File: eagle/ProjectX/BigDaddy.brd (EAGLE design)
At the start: 100 x 100 mm, 180 parts, among them U10 TC4427AEOA, U11 TC4427AEOA, U12 TC4427AEOA, U13 TC4427AEOA, U19 TC4427AEOA, U20 TC4427AEOA, U21 TC4427AEOA, U22 TC4427AEOA, U23 TC4427AEOA, U24 TC4427AEOA, U25 TC4427AEOA, U26 TC4427AEOA, U27 TC4427AEOA, U28 TC4427AEOA, U29 TC4427AEOA, U3 TC4427AEOA, U30 TC4427AEOA, U31 TC4427AEOA, U32 TC4427AEOA, U34 TC4427AEOA, U35 TC4427AEOA, U36 TC4427AEOA, U37 TC4427AEOA, U38 TC4427AEOA, U39 TC4427AEOA, U4 TC4427AEOA, U40 TC4427AEOA, U41 TC4427AEOA, U42 TC4427AEOA, U43 TC4427AEOA, U44 TC4427AEOA, U45 TC4427AEOA, U5 TC4427AEOA, U55 TC4427AEOA, U56 TC4427AEOA, U57 TC4427AEOA, U58 TC4427AEOA, U59 TC4427AEOA, U60 TC4427AEOA, U61 TC4427AEOA, U62 TC4427AEOA, U63 TC4427AEOA, U7 TC4427AEOA, U9 TC4427AEOA

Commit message: More work on the board
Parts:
- moved J2 23.0 mm to (24.0, 98.5), turned to 0 degrees
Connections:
- new net 1: DIP1.2, U28.4
- new net 2: DIP1.4, U28.2
- new net 3: DIP1.3, U29.4
- new net 4: DIP1.5, U29.2
- new net N$1: DIP1.203, J2.1
- new net N$13: DIP1.190, J2.5
- new net N$14: DIP1.187, J2.6
- new net N$17: DIP1.185, J2.7
- new net N$18: DIP1.180, J2.8
- new net N$2: DIP1.200, J2.2
- new net N$29: DIP1.178, J2.9
- new net N$3: DIP1.197, J2.3
- new net N$30: DIP1.172, J2.10
- new net N$4: DIP1.193, J2.4
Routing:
- net 3: track 0.00 -> 16.4 mm
- net 1: track 0.00 -> 16.1 mm
- net 2: track 0.00 -> 10.3 mm
- net 4: track 0.00 -> 9.98 mm
- net N$30: track 0.00 -> 6.66 mm
- net N$29: track 0.00 -> 6.43 mm
- net N$18: track 0.00 -> 5.87 mm
- net N$17: track 0.00 -> 4.88 mm
- net N$14: track 0.00 -> 4.22 mm
- net N$3: track 0.00 -> 4.18 mm
- net N$13: track 0.00 -> 3.99 mm
- net N$4: track 0.00 -> 3.77 mm
- net N$2: track 0.00 -> 3.64 mm
- net N$1: track 0.00 -> 3.10 mm
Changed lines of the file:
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@@
 <element name="J1" library="SparkFun-Connectors" library_urn="urn:adsk.eagle:library:513" package="1X02_LOCK_LONGPADS" package3d_urn="urn:adsk.eagle:package:38047/1" value="" x="68.75" y="10" rot="R180"/>
 <element name="U$1" library="Parts" package="OKI-78SR-HORIZ" value="OKI-78SR" x="67.5" y="30" rot="R180"/>
-<element name="J2" library="SparkFun-Connectors" library_urn="urn:adsk.eagle:library:513" package="1X10" package3d_urn="urn:adsk.eagle:package:38157/1" value="" x="47" y="98.5" rot="R180">
-<attribute name="PROD_ID" value="CONN-11563" x="47" y="98.5" size="1.778" layer="27" rot="R180" display="off"/>
+<element name="J2" library="SparkFun-Connectors" library_urn="urn:adsk.eagle:library:513" package="1X10" package3d_urn="urn:adsk.eagle:package:38157/1" value="" x="24" y="98.5">
+<attribute name="PROD_ID" value="CONN-11563" x="24" y="98.5" size="1.778" layer="27" display="off"/>
 </element>
 </elements>
@@
 <wire x1="50" y1="82.6378" x2="50" y2="82.5" width="0.508" layer="1"/>
 </signal>
+<signal name="N$1">
+<contactref element="J2" pad="1"/>
+<contactref element="DIP1" pad="203"/>
+<wire x1="24" y1="98.5" x2="24" y2="95.4" width="0.254" layer="1"/>
+</signal>
+<signal name="N$2">
+<contactref element="J2" pad="2"/>
+<contactref element="DIP1" pad="200"/>
+<wire x1="26.54" y1="98.5" x2="26" y2="98.5" width="0.254" layer="1"/>
+<wire x1="26" y1="98.5" x2="26" y2="95.4" width="0.254" layer="1"/>
+</signal>
+<signal name="N$3">
+<contactref element="J2" pad="3"/>
+<contactref element="DIP1" pad="197"/>
+<wire x1="29.08" y1="98.5" x2="28" y2="98.5" width="0.254" layer="1"/>
+<wire x1="28" y1="98.5" x2="28" y2="95.4" width="0.254" layer="1"/>
+</signal>
+<signal name="N$4">
+<contactref element="J2" pad="4"/>
+<contactref element="DIP1" pad="193"/>
+<wire x1="31.62" y1="98.5" x2="30" y2="96.88" width="0.254" layer="1"/>
+<wire x1="30" y1="96.88" x2="30" y2="95.4" width="0.254" layer="1"/>
+</signal>
+<signal name="N$13">
+<contactref element="J2" pad="5"/>
+<contactref element="DIP1" pad="190"/>
+<wire x1="34.16" y1="98.5" x2="32" y2="96.34" width="0.254" layer="1"/>
+<wire x1="32" y1="96.34" x2="32" y2="95.4" width="0.254" layer="1"/>
+</signal>
+<signal name="N$14">
+<contactref element="J2" pad="6"/>
+<contactref element="DIP1" pad="187"/>
+<wire x1="36.7" y1="98.5" x2="34" y2="95.8" width="0.254" layer="1"/>
+<wire x1="34" y1="95.8" x2="34" y2="95.4" width="0.254" layer="1"/>
+</signal>
+<signal name="N$17">
+<contactref element="J2" pad="7"/>
+<contactref element="DIP1" pad="185"/>
+<wire x1="39.24" y1="98.5" x2="38.49605625" y2="98.5" width="0.254" layer="1"/>
+<wire x1="36" y1="96.00394375" x2="36" y2="95.4" width="0.254" layer="1"/>
+<wire x1="38.49605625" y1="98.5" x2="36" y2="96.00394375" width="0.254" layer="1"/>
+</signal>
+<signal name="N$18">
+<contactref element="J2" pad="8"/>
+<contactref element="DIP1" pad="180"/>
+<wire x1="41.78" y1="98.5" x2="41.03605625" y2="98.5" width="0.254" layer="1"/>
+<wire x1="38" y1="96.77078125" x2="38" y2="95.4" width="0.254" layer="1"/>
+<wire x1="38.45921875" y1="97.23" x2="38" y2="96.77078125" width="0.254" layer="1"/>
+<wire x1="41.03605625" y1="98.5" x2="39.76605625" y2="97.23" width="0.254" layer="1"/>
+<wire x1="39.76605625" y1="97.23" x2="38.45921875" y2="97.23" width="0.254" layer="1"/>
+</signal>
+<signal name="N$29">
+<contactref element="J2" pad="9"/>
+<contactref element="DIP1" pad="178"/>
+<wire x1="40" y1="96.8173625" x2="40" y2="95.4" width="0.254" layer="1"/>
+<wire x1="44.32" y1="98.5" x2="43.57605625" y2="98.5" width="0.254" layer="1"/>
+<wire x1="40.4126375" y1="97.23" x2="40" y2="96.8173625" width="0.254" layer="1"/>
+<wire x1="43.57605625" y1="98.5" x2="42.30605625" y2="97.23" width="0.254" layer="1"/>
+<wire x1="42.30605625" y1="97.23" x2="40.4126375" y2="97.23" width="0.254" layer="1"/>
+</signal>
+<signal name="N$30">
+<contactref element="J2" pad="10"/>
+<contactref element="DIP1" pad="172"/>
+<wire x1="46.86" y1="98.5" x2="46.11605625" y2="98.5" width="0.254" layer="1"/>
+<wire x1="42" y1="96.2773625" x2="42" y2="95.4" width="0.254" layer="1"/>
+<wire x1="46.11605625" y1="98.5" x2="44.84605625" y2="97.23" width="0.254" layer="1"/>
+<wire x1="44.84605625" y1="97.23" x2="42.9526375" y2="97.23" width="0.254" layer="1"/>
+<wire x1="42.9526375" y1="97.23" x2="42" y2="96.2773625" width="0.254" layer="1"/>
+</signal>
+<signal name="1">
+<contactref element="U28" pad="4"/>
+<contactref element="DIP1" pad="2"/>
+<wire x1="20.8302" y1="94.163225" x2="20.636775" y2="93.9698" width="0.254" layer="1"/>
+<wire x1="20.636775" y1="93.9698" x2="19.363225" y2="93.9698" width="0.254" layer="1"/>
+<wire x1="9.095" y1="95.4" x2="9.095" y2="97.3622" width="0.254" layer="1"/>
+<wire x1="22" y1="95.4" x2="20.8302" y2="94.2302" width="0.254" layer="1"/>
+<wire x1="20.8302" y1="94.2302" x2="20.8302" y2="94.163225" width="0.254" layer="1"/>
+<wire x1="19.363225" y1="93.9698" x2="18.390225" y2="94.9428" width="0.254" layer="1"/>
+<wire x1="9.5522" y1="94.9428" x2="9.095" y2="95.4" width="0.254" layer="1"/>
+<wire x1="18.390225" y1="94.9428" x2="9.5522" y2="94.9428" width="0.254" layer="1"/>
+</signal>
+<signal name="2">
+<contactref element="U28" pad="2"/>
+<contactref element="DIP1" pad="4"/>
+<wire x1="20" y1="95.4" x2="11.635" y2="95.4" width="0.254" layer="1"/>
+<wire x1="11.635" y1="95.4" x2="11.635" y2="97.3622" width="0.254" layer="1"/>
+</signal>
+<signal name="3">
+<contactref element="U29" pad="4"/>
+<contactref element="DIP1" pad="3"/>
+<wire x1="20.8302" y1="91.836775" x2="20.636775" y2="92.0302" width="0.254" layer="1"/>
+<wire x1="20" y1="92.0302" x2="19.363225" y2="92.0302" width="0.254" layer="1"/>
+<wire x1="20" y1="92.0302" x2="20.636775" y2="92.0302" width="0.254" layer="1"/>
+<wire x1="22" y1="90.6" x2="20.8302" y2="91.7698" width="0.254" layer="1"/>
+<wire x1="20.8302" y1="91.7698" x2="20.8302" y2="91.836775" width="0.254" layer="1"/>
+<wire x1="9.095" y1="87.3622" x2="9.7554" y2="88.0226" width="0.254" layer="1"/>
+<wire x1="9.7554" y1="88.0226" x2="9.7554" y2="88.489575" width="0.254" layer="1"/>
+<wire x1="9.7554" y1="88.489575" x2="11.765825" y2="90.5" width="0.254" layer="1"/>
+<wire x1="11.765825" y1="90.5" x2="17" y2="90.5" width="0.254" layer="1"/>
+<wire x1="17" y1="90.5" x2="18.5302" y2="92.0302" width="0.254" layer="1"/>
+<wire x1="18.5302" y1="92.0302" x2="20" y2="92.0302" width="0.254" layer="1"/>
+</signal>
+<signal name="4">
+<contactref element="U29" pad="2"/>
+<contactref element="DIP1" pad="5"/>
+<wire x1="12.2954" y1="88.489575" x2="12.2954" y2="88.0226" width="0.254" layer="1"/>
+<wire x1="12.2954" y1="88.0226" x2="11.635" y2="87.3622" width="0.254" layer="1"/>
+<wire x1="13.348625" y1="89.5428" x2="12.2954" y2="88.489575" width="0.254" layer="1"/>
+<wire x1="20" y1="90.6" x2="18.9428" y2="89.5428" width="0.254" layer="1"/>
+<wire x1="18.9428" y1="89.5428" x2="13.348625" y2="89.5428" width="0.254" layer="1"/>
+</signal>
 </signals>

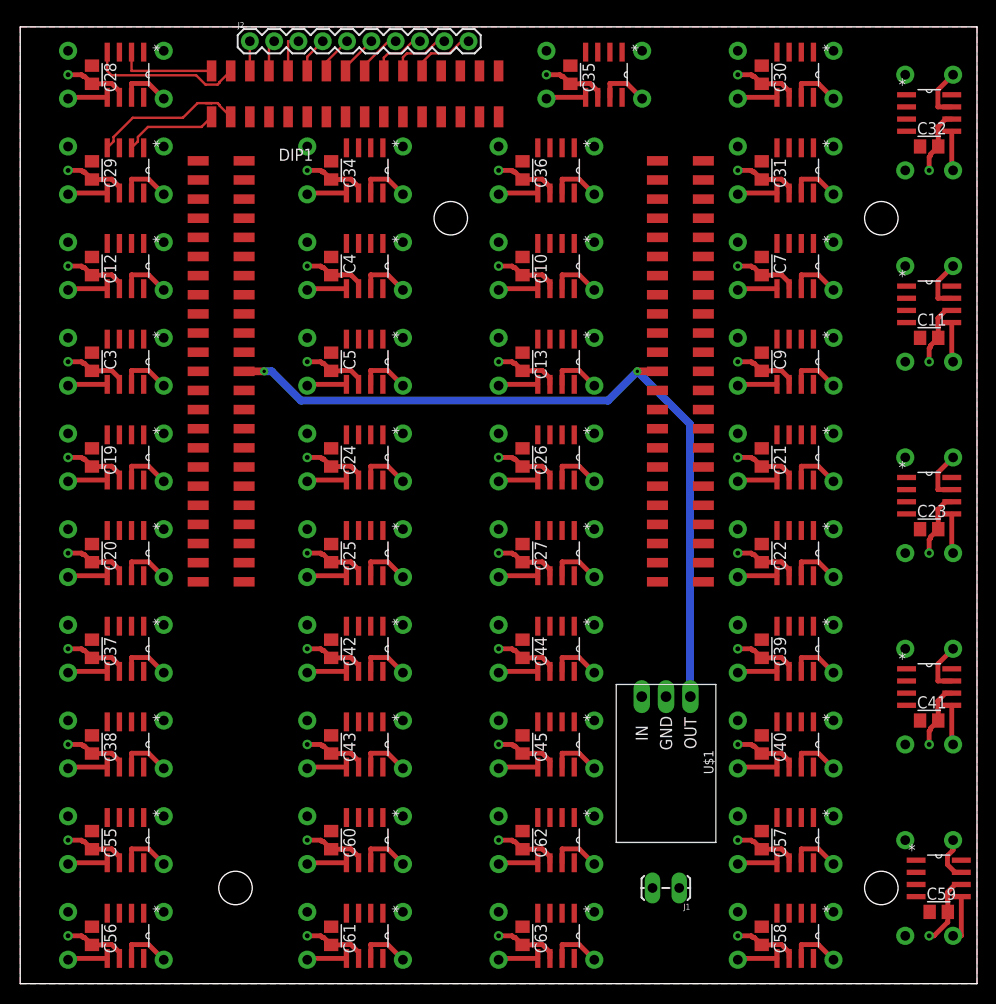
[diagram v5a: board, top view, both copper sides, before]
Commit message: Routed 16 channels
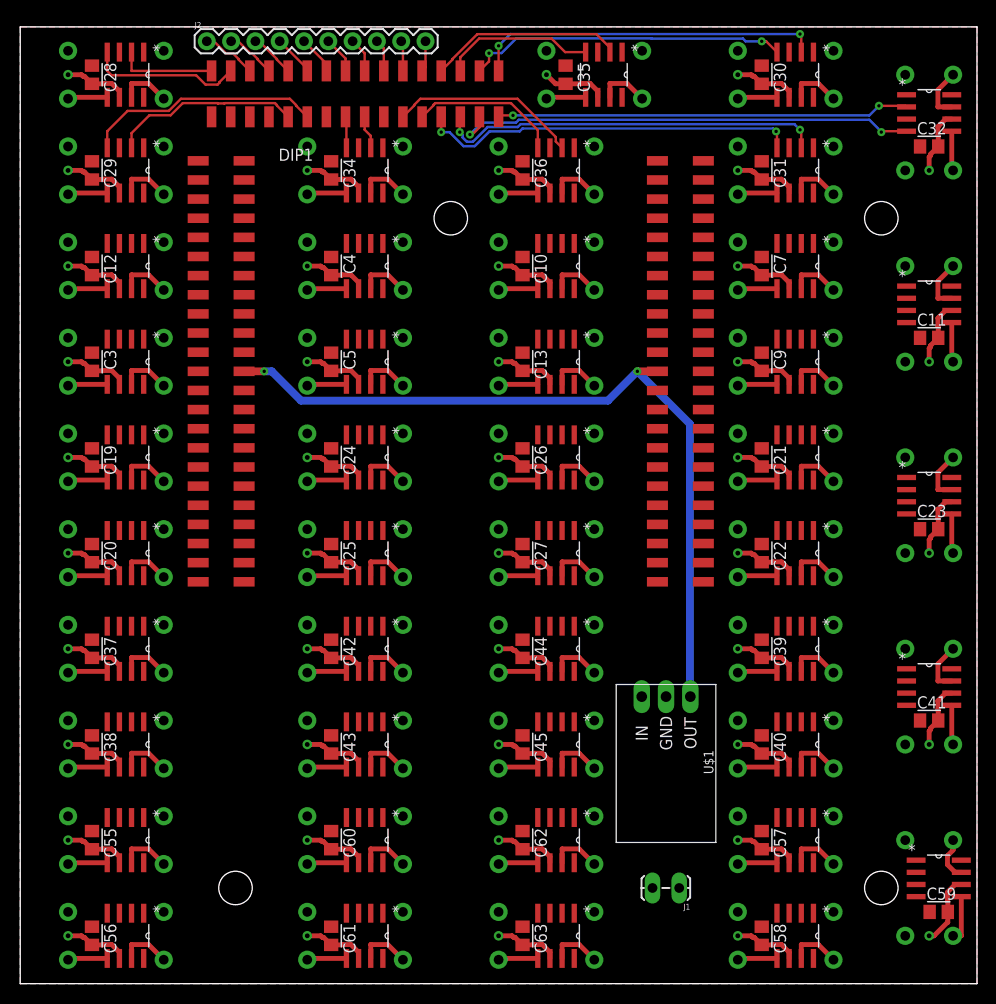
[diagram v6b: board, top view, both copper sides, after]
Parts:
- moved J2 4.50 mm to (19.5, 98.5)
- moved C35 0.50 mm to (57.0, 95.0)
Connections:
- new net 10: DIP1.189, U34.4
- new net 11: DIP1.186, U34.2
- new net 12: DIP1.177, U36.4
- new net 13: DIP1.179, U36.2
- new net 14: DIP1.171, U31.4
- new net 15: DIP1.167, U31.2
- new net 16: DIP1.164, U32.4
- new net 5: DIP1.163, U30.4
- new net 6: DIP1.161, U30.2
- new net 7: DIP1.162, U32.2
- new net 8: DIP1.196, U29.4
- new net 9: DIP1.199, U29.2
- net 3: now also DIP1.165, U35.4; no longer DIP1.3, U29.4
- net 4: now also DIP1.168, U35.2; no longer DIP1.5, U29.2
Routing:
- net 16: track 0.00 -> 49.3 mm, vias 0 -> 2
- net 7: track 0.00 -> 43.4 mm, vias 0 -> 2
- net 15: track 0.00 -> 40.7 mm, vias 0 -> 2
- net 14: track 0.00 -> 39.9 mm, vias 0 -> 2
- net 6: track 0.00 -> 36.6 mm, vias 0 -> 2
- net 5: track 0.00 -> 33.6 mm, vias 0 -> 2
- net 8: track 0.00 -> 24.9 mm
- net 9: track 0.00 -> 19.9 mm
- net 13: track 0.00 -> 19.9 mm
- net 12: track 0.00 -> 15.8 mm
- net 4: track 9.98 -> 20.3 mm
- net 11: track 0.00 -> 3.50 mm
- net N$30: track 6.66 -> 3.25 mm
- net 10: track 0.00 -> 3.28 mm
- net N$29: track 6.43 -> 3.17 mm
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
